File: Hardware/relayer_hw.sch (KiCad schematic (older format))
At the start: 57 parts, among them J1 BOOT0, J2 AC_OUT, J3 STLink, J4 AC_IN, Q1 2N7002, SW1 NRST, SW2 USR_SW, U1 STM32WB55, U2 902-9040, U3 LM1117-3.3, Y1 Crystal, Y2 Crystal_GND23

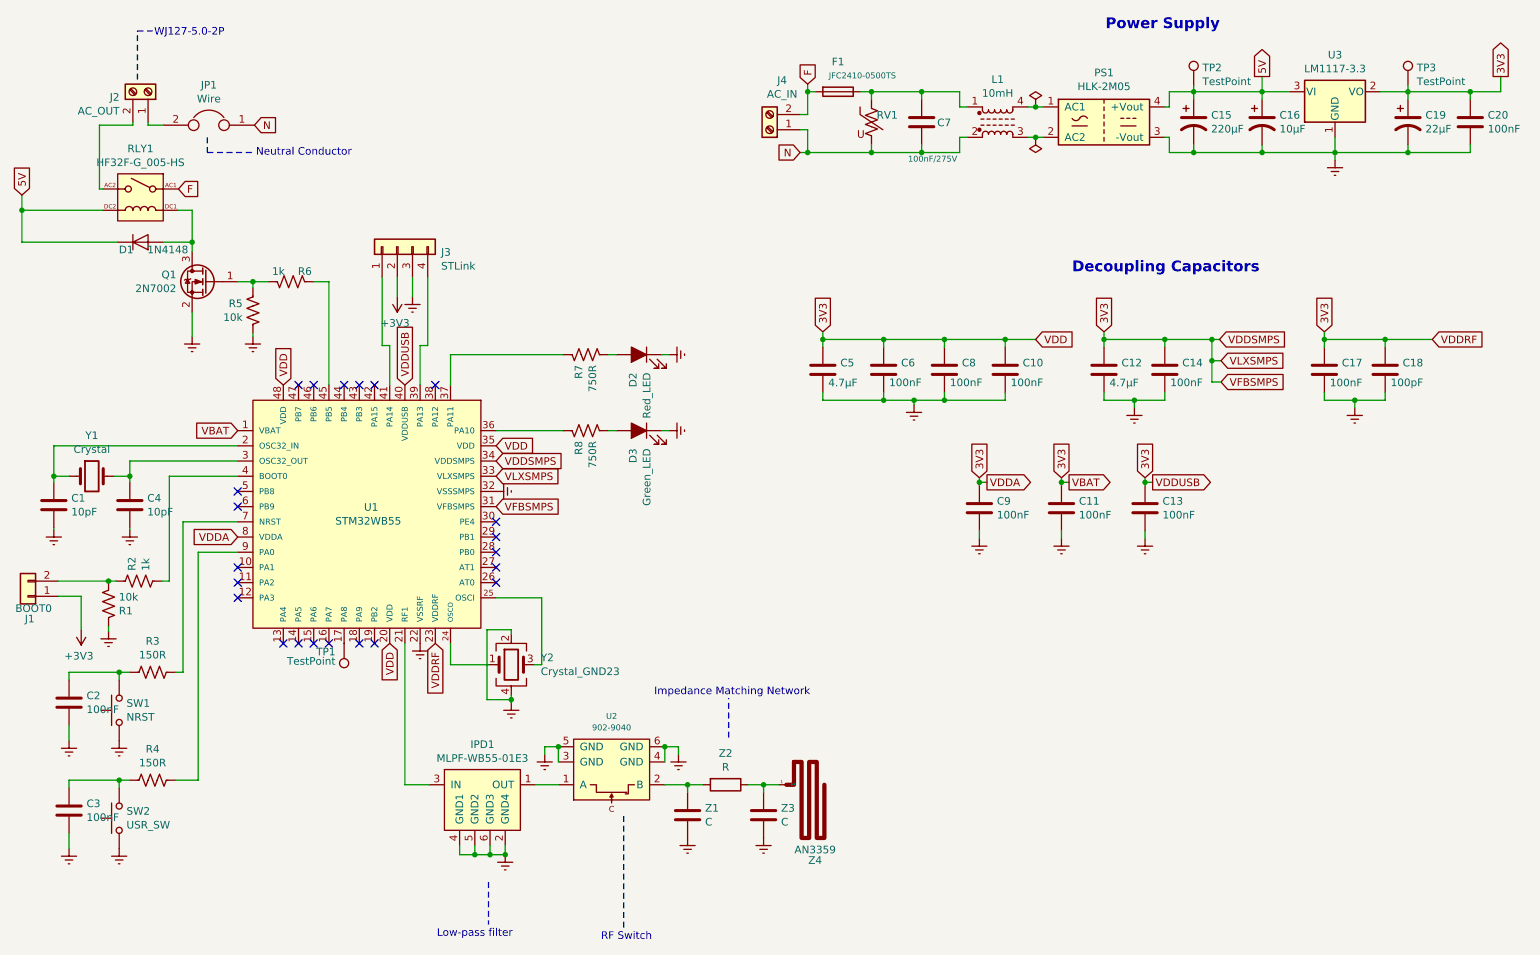
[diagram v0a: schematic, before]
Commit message: Netlist gerada/ Correncao de nets/ Inicio do layout
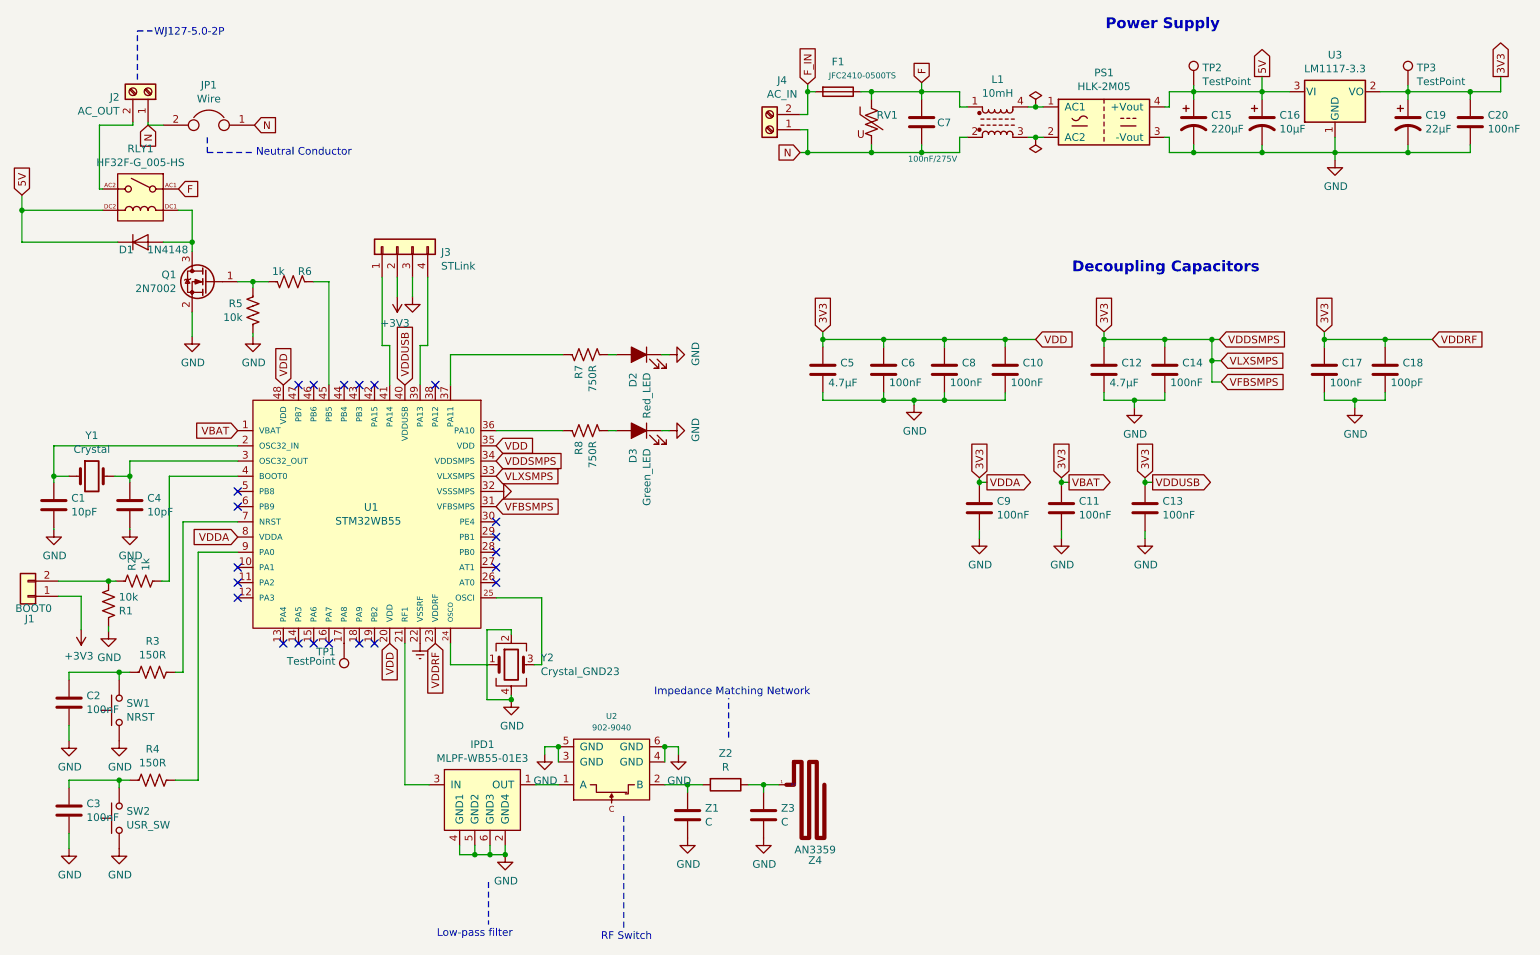
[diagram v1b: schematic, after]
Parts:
- C4: footprint (none) -> Capacitor_SMD:C_0402_1005Metric
- J2: footprint (none) -> TerminalBlock:TerminalBlock_bornier-2_P5.08mm
- J4: footprint TerminalBlock:TerminalBlock_bornier-2_P5.08mm -> Usr_pretty_lib:TerminalBlock_bornier-2_P5.08mm
- JP1: footprint (none) -> Usr_pretty_lib:neutral_wire
- SW1: footprint (none) -> Usr_pretty_lib:1TS002B-1900-4300-CT
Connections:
- net F: now also C7.1, F1.1, L1.1, RV1.1; no longer F1.2, J4.2 (Pin_2)
- net N: now also J2.1 (Pin_1), JP1.2
- net GND: now reaches Q1.2 (S)
- net GND: now also C1.2, C10.2, C11.2, C12.2, C13.2, C14.2, C15.2, C16.2, C17.2, C18.2, C19.2, C2.1, C20.2, C3.1, C4.2, C5.2, C6.2, C8.2, C9.2, D2.1 (K), D3.1 (K), IPD1.2 (GND4), IPD1.4 (GND1), IPD1.5 (GND2), IPD1.6 (GND3), J3.3 (Pin_3), PS1.3 (-Vout), R1.2, R5.2, SW1.2, SW2.2, U1.32 (VSSSMPS), U2.3 (GND), U2.4 (GND), U2.5 (GND), U2.6 (GND), U3.1 (GND), Y2.2, Y2.4, Z1.2, Z3.2
- new net F_IN: F1.2, J4.2 (Pin_2)

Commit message: Correção nos cristais/Posicionamento dos componentes em andamento
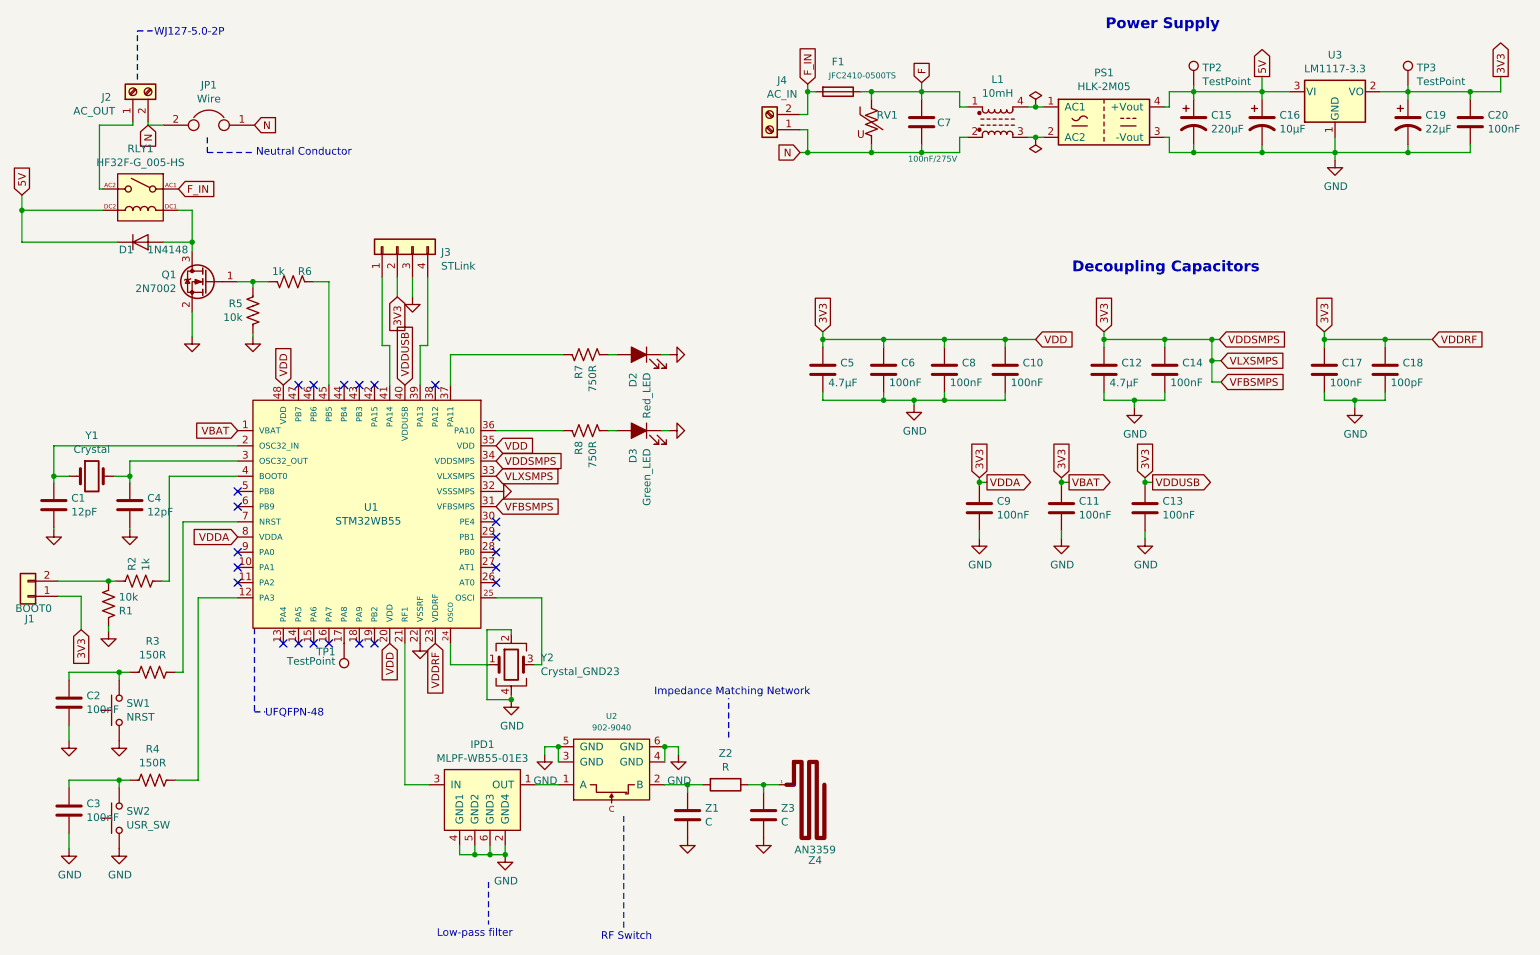
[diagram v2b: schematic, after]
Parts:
- C1, C4: value 10pF -> 12pF
- F1: footprint Fuse:Fuse_2010_5025Metric_Pad1.52x2.65mm_HandSolder -> Usr_pretty_lib:Fuse_2010_5025Metric_Pad1.52x2.65mm_HandSolder
- J2: footprint TerminalBlock:TerminalBlock_bornier-2_P5.08mm -> Usr_pretty_lib:TerminalBlock_bornier-2_P5.08mm
- TP1: footprint TestPoint:TestPoint_Loop_D2.54mm_Drill1.5mm_Beaded -> Connector_PinHeader_2.54mm:PinHeader_1x01_P2.54mm_Vertical
- Y1: footprint Crystal:Crystal_SMD_2012-2Pin_2.0x1.2mm_HandSoldering -> Usr_pretty_lib:Crystal_SMD_2012-2Pin_2.0x1.2mm_HandSoldering
- Y2: footprint Crystal:Crystal_SMD_2016-4Pin_2.0x1.6mm -> Usr_pretty_lib:Crystal_SMD_3225-4Pin_3.2x2.5mm_HandSoldering
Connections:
- net 3V3: now also J1.1 (Pin_1), J3.2 (Pin_2)
- net F: no longer RLY1.AC1
- net F_IN: now also RLY1.AC1
- net GND: now also U1.22 (VSSRF)
- net N: now also J2.2 (Pin_2); no longer J2.1 (Pin_1)
- net at RLY1.AC2: now also J2.1 (Pin_1); no longer J2.2 (Pin_2)
- net at U1.12 (PA3): now also R4.1
- net at U1.9 (PA0): no longer R4.1
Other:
- note added: "UFQFPN-48"
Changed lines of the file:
@@
 $EndDescr
-$Comp
-L Regulator_Linear:LM1117-3.3 U3
-U 1 1 60667377
-P 9780 1400
-F 0 "U3" H 9780 1642 50  0000 C CNN
-F 1 "LM1117-3.3" H 9780 1551 50  0000 C CNN
-F 2 "Package_TO_SOT_SMD:SOT-223" H 9780 1400 50  0001 C CNN
-F 3 "https://www.ti.com/lit/ds/symlink/lm1117.pdf?HQS=dis-mous-null-mousermode-dsf-pf-null-wwe&DCM=yes&ref_url=https%3A%2F%2Fwww.mouser.es%2F&distId=26" H 9780 1400 50  0001 C CNN
-	1    9780 1400
-	1    0    0    -1
-$EndComp
 $Comp
 L Device:CP1 C16
@@
 P 1350 4120
 F 0 "C1" H 1465 4166 50  0000 L CNN
-F 1 "10pF" H 1465 4075 50  0000 L CNN
+F 1 "12pF" H 1465 4075 50  0000 L CNN
 F 2 "Capacitor_SMD:C_0402_1005Metric" H 1388 3970 50  0001 C CNN
 F 3 "https://br.mouser.com/datasheet/2/40/AVX_01005_Ultra_Miniature_Capacitors-1920440.pdf" H 1350 4120 50  0001 C CNN
@@
 P 1850 4120
 F 0 "C4" H 1965 4166 50  0000 L CNN
-F 1 "10pF" H 1965 4075 50  0000 L CNN
+F 1 "12pF" H 1965 4075 50  0000 L CNN
 F 2 "Capacitor_SMD:C_0402_1005Metric" H 1888 3970 50  0001 C CNN
 F 3 "~" H 1850 4120 50  0001 C CNN
@@
 F 0 "Y1" H 1600 4198 50  0000 C CNN
 F 1 "Crystal" H 1600 4107 50  0000 C CNN
-F 2 "Crystal:Crystal_SMD_2012-2Pin_2.0x1.2mm_HandSoldering" H 1600 3930 50  0001 C CNN
+F 2 "Usr_pretty_lib:Crystal_SMD_2012-2Pin_2.0x1.2mm_HandSoldering" H 1600 3930 50  0001 C CNN
 F 3 "https://br.mouser.com/datasheet/2/905/c_NX2012SA-STD-MUB-1_e-1317508.pdf" H 1600 3930 50  0001 C CNN
 	1    1600 3930
@@
 F 0 "Y2" H 4554 5216 50  0000 L CNN
 F 1 "Crystal_GND23" H 4554 5125 50  0000 L CNN
-F 2 "Crystal:Crystal_SMD_2016-4Pin_2.0x1.6mm" H 4360 5170 50  0001 C CNN
+F 2 "Usr_pretty_lib:Crystal_SMD_3225-4Pin_3.2x2.5mm_HandSoldering" H 4360 5170 50  0001 C CNN
 F 3 "https://br.mouser.com/datasheet/2/122/ECX_1637B-1649431.pdf" H 4360 5170 50  0001 C CNN
 	1    4360 5170
@@
 	0    -1   -1   0
 $EndComp
-$Comp
-L power:+3V3 #PWR012
-U 1 1 60898688
-P 3610 2750
-F 0 "#PWR012" H 3610 2600 50  0001 C CNN
-F 1 "+3V3" H 3625 2923 50  0000 C CNN
-F 2 "" H 3610 2750 50  0001 C CNN
-F 3 "" H 3610 2750 50  0001 C CNN
-	1    3610 2750
-	-1   0    0    1
-$EndComp
 Wire Wire Line
 	3710 2620 3710 2750
@@
 	-1   0    0    -1
 $EndComp
-$Comp
-L power:+3V3 #PWR05
-U 1 1 60A6FD6F
-P 1530 4940
-F 0 "#PWR05" H 1530 4790 50  0001 C CNN
-F 1 "+3V3" H 1545 5113 50  0000 C CNN
-F 2 "" H 1530 4940 50  0001 C CNN
-F 3 "" H 1530 4940 50  0001 C CNN
-	1    1530 4940
-	-1   0    0    1
-$EndComp
 Wire Wire Line
 	1380 4620 1710 4620
@@
 Wire Wire Line
 	1530 4720 1530 4940
-Wire Wire Line
-	2560 4430 2300 4430
-Wire Wire Line
-	2300 4430 2300 5930
 Wire Wire Line
 	2200 4230 2200 5220
@@
 $EndComp
 Text GLabel 2170 2040 2    50   Input ~ 0
-F
+F_IN
 Wire Wire Line
 	1870 1620 1870 1600
@@
 Wire Wire Line
 	1670 2040 1650 2040
-$Comp
-L Connector:Screw_Terminal_01x02 J2
-U 1 1 60704D74
-P 1970 1400
-F 0 "J2" V 1934 1212 50  0000 R CNN
-F 1 "AC_OUT" V 1843 1212 50  0000 R CNN
-F 2 "TerminalBlock:TerminalBlock_bornier-2_P5.08mm" H 1970 1400 50  0001 C CNN
-F 3 "~" H 1970 1400 50  0001 C CNN
-	1    1970 1400
-	0    1    -1   0
-$EndComp
 Connection ~ 1140 2180
 Wire Wire Line
@@
 	5000 3130 5050 3130
 $Comp
-L power:Earth #PWR014
-U 1 1 609465CA
-P 3760 5030
-F 0 "#PWR014" H 3760 4780 50  0001 C CNN
-F 1 "Earth" H 3760 4880 50  0001 C CNN
-F 2 "" H 3760 5030 50  0001 C CNN
-F 3 "~" H 3760 5030 50  0001 C CNN
-	1    3760 5030
-	1    0    0    -1
-$EndComp
-$Comp
 L Device:C Z1
 U 1 1 609A98E6
@@
 F 1 "2N7002" H 2564 2605 50  0000 L CNN
 F 2 "Package_TO_SOT_SMD:SOT-23" H 2560 2575 50  0001 L CIN
-F 3 "https://www.fairchildsemi.com/datasheets/2N/2N7002.pdf" H 2360 2650 50  0001 L CNN
+F 3 "https://www.mouser.com/datasheet/2/916/2N7002NXAK-1651343.pdf" H 2360 2650 50  0001 L CNN
 	1    2360 2650
 	-1   0    0    -1
@@
 F 0 "F1" V 6313 1400 50  0000 C CNN
 F 1 "JFC2410-0500TS" V 6404 1339 39  0000 L CNN
-F 2 "Fuse:Fuse_2010_5025Metric_Pad1.52x2.65mm_HandSolder" V 6440 1400 50  0001 C CNN
+F 2 "Usr_pretty_lib:Fuse_2010_5025Metric_Pad1.52x2.65mm_HandSolder" V 6440 1400 50  0001 C CNN
 F 3 "https://datasheet.lcsc.com/lcsc/1809211427_Shenzhen-JDT-Fuse-JFC2410-0500TS_C136377.pdf" H 6510 1400 50  0001 C CNN
 	1    6510 1400
@@
 F 0 "TP1" H 3203 5056 50  0000 R BNN
 F 1 "TestPoint" H 3203 5147 50  0000 R CNN
-F 2 "TestPoint:TestPoint_Loop_D2.54mm_Drill1.5mm_Beaded" H 3460 5030 50  0001 C CNN
+F 2 "Connector_PinHeader_2.54mm:PinHeader_1x01_P2.54mm_Vertical" H 3460 5030 50  0001 C CNN
 F 3 "~" H 3460 5030 50  0001 C CNN
 	1    3260 5030
@@
 NoConn ~ 2560 4530
 NoConn ~ 2560 4630
-NoConn ~ 2560 4730
 Text GLabel 10870 1300 1    50   Output ~ 0
 3V3
@@
 P 1350 4280
 F 0 "#PWR0101" H 1350 4030 50  0001 C CNN
-F 1 "GND" H 1355 4107 50  0000 C CNN
+F 1 "GND" H 1355 4107 50  0001 C CNN
 F 2 "" H 1350 4280 50  0001 C CNN
 F 3 "" H 1350 4280 50  0001 C CNN
@@
 P 1850 4280
 F 0 "#PWR0102" H 1850 4030 50  0001 C CNN
-F 1 "GND" H 1855 4107 50  0000 C CNN
+F 1 "GND" H 1855 4107 50  0001 C CNN
 F 2 "" H 1850 4280 50  0001 C CNN
 F 3 "" H 1850 4280 50  0001 C CNN
@@
 P 1710 4950
 F 0 "#PWR0103" H 1710 4700 50  0001 C CNN
-F 1 "GND" H 1715 4777 50  0000 C CNN
+F 1 "GND" H 1715 4777 50  0001 C CNN
 F 2 "" H 1710 4950 50  0001 C CNN
 F 3 "" H 1710 4950 50  0001 C CNN
@@
 P 5520 6310
 F 0 "#PWR0107" H 5520 6060 50  0001 C CNN
-F 1 "GND" H 5525 6137 50  0000 C CNN
+F 1 "GND" H 5525 6137 50  0001 C CNN
 F 2 "" H 5520 6310 50  0001 C CNN
 F 3 "" H 5520 6310 50  0001 C CNN
@@
 P 6020 6310
 F 0 "#PWR0108" H 6020 6060 50  0001 C CNN
-F 1 "GND" H 6025 6137 50  0000 C CNN
+F 1 "GND" H 6025 6137 50  0001 C CNN
 F 2 "" H 6020 6310 50  0001 C CNN
 F 3 "" H 6020 6310 50  0001 C CNN
@@
 P 5400 3130
 F 0 "#PWR0112" H 5400 2880 50  0001 C CNN
-F 1 "GND" H 5405 2957 50  0000 C CNN
+F 1 "GND" H 5405 2957 50  0001 C CNN
 F 2 "" H 5400 3130 50  0001 C CNN
 F 3 "" H 5400 3130 50  0001 C CNN
@@
 P 5400 3630
 F 0 "#PWR0113" H 5400 3380 50  0001 C CNN
-F 1 "GND" H 5405 3457 50  0000 C CNN
+F 1 "GND" H 5405 3457 50  0001 C CNN
 F 2 "" H 5400 3630 50  0001 C CNN
 F 3 "" H 5400 3630 50  0001 C CNN
@@
 P 2260 3010
 F 0 "#PWR0115" H 2260 2760 50  0001 C CNN
-F 1 "GND" H 2265 2837 50  0000 C CNN
+F 1 "GND" H 2265 2837 50  0001 C CNN
 F 2 "" H 2260 3010 50  0001 C CNN
 F 3 "" H 2260 3010 50  0001 C CNN
@@
 P 2660 3010
 F 0 "#PWR0116" H 2660 2760 50  0001 C CNN
-F 1 "GND" H 2665 2837 50  0000 C CNN
+F 1 "GND" H 2665 2837 50  0001 C CNN
 F 2 "" H 2660 3010 50  0001 C CNN
 F 3 "" H 2660 3010 50  0001 C CNN
@@
 P 1450 5670
 F 0 "#PWR0124" H 1450 5420 50  0001 C CNN
-F 1 "GND" H 1455 5497 50  0000 C CNN
+F 1 "GND" H 1455 5497 50  0001 C CNN
 F 2 "" H 1450 5670 50  0001 C CNN
 F 3 "" H 1450 5670 50  0001 C CNN
@@
 P 1780 5670
 F 0 "#PWR0125" H 1780 5420 50  0001 C CNN
-F 1 "GND" H 1785 5497 50  0000 C CNN
+F 1 "GND" H 1785 5497 50  0001 C CNN
 F 2 "" H 1780 5670 50  0001 C CNN
 F 3 "" H 1780 5670 50  0001 C CNN
@@
 Text GLabel 1970 1620 3    50   Input ~ 0
 N
+Text GLabel 1530 4940 3    50   Input ~ 0
+3V3
+Text GLabel 3610 2750 3    50   Input ~ 0
+3V3
+$Comp
+L Connector:Screw_Terminal_01x02 J2
+U 1 1 60704D74
+P 1870 1400
+F 0 "J2" V 1834 1606 50  0000 R CNN
+F 1 "AC_OUT" V 1743 1792 50  0000 R CNN
+F 2 "Usr_pretty_lib:TerminalBlock_bornier-2_P5.08mm" H 1870 1400 50  0001 C CNN
+F 3 "~" H 1870 1400 50  0001 C CNN
+	1    1870 1400
+	0    -1   -1   0
+$EndComp
+$Comp
+L Regulator_Linear:LM1117-3.3 U3
+U 1 1 60667377
+P 9780 1400
+F 0 "U3" H 9780 1642 50  0000 C CNN
+F 1 "LM1117-3.3" H 9780 1551 50  0000 C CNN
+F 2 "Package_TO_SOT_SMD:SOT-223" H 9780 1400 50  0001 C CNN
+F 3 "https://www.ti.com/lit/ds/symlink/lm1117.pdf?HQS=dis-mous-null-mousermode-dsf-pf-null-wwe&DCM=yes&ref_url=https%3A%2F%2Fwww.mouser.es%2F&distId=26" H 9780 1400 50  0001 C CNN
+	1    9780 1400
+	1    0    0    -1
+$EndComp
+$Comp
+L power:GND #PWR0127
+U 1 1 60C490E9
+P 3760 5030
+F 0 "#PWR0127" H 3760 4780 50  0001 C CNN
+F 1 "GND" H 3765 4857 50  0001 C CNN
+F 2 "" H 3760 5030 50  0001 C CNN
+F 3 "" H 3760 5030 50  0001 C CNN
+	1    3760 5030
+	1    0    0    -1
+$EndComp
+Wire Notes Line
+	2670 4930 2670 5480
+Wire Notes Line
+	2670 5480 2740 5480
+Text Notes 2740 5520 0    50   ~ 0
+UFQFPN-48
+NoConn ~ 2560 4430
+Wire Wire Line
+	2300 5930 2300 4730
+Wire Wire Line
+	2300 4730 2560 4730
 $EndSCHEMATC
